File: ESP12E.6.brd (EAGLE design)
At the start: 36.6 x 36.6 mm, 64 parts, among them CN2 1X4-BIG, J1 1X2-3.5MM, J4 1X2-3.5MM, U1 A5984

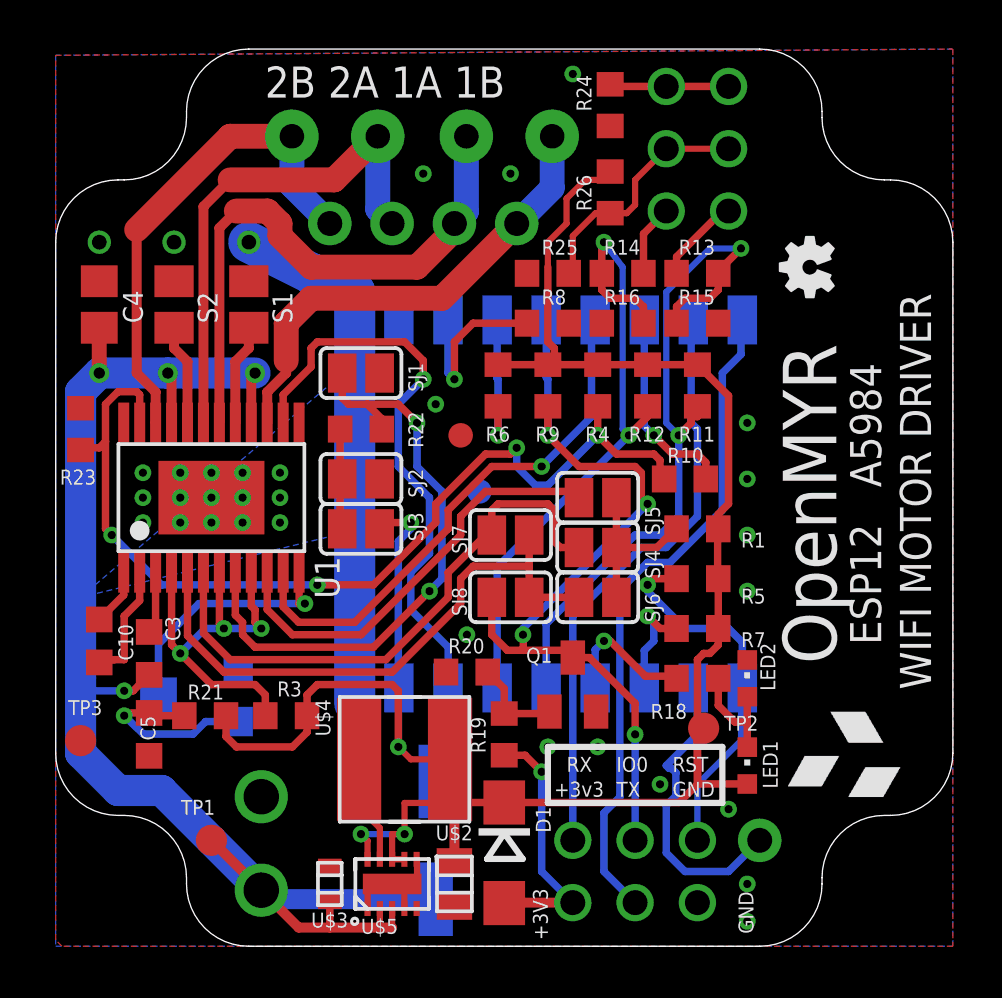
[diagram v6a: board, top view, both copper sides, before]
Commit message: A5984 QFN24
Layout with QFN24 driver
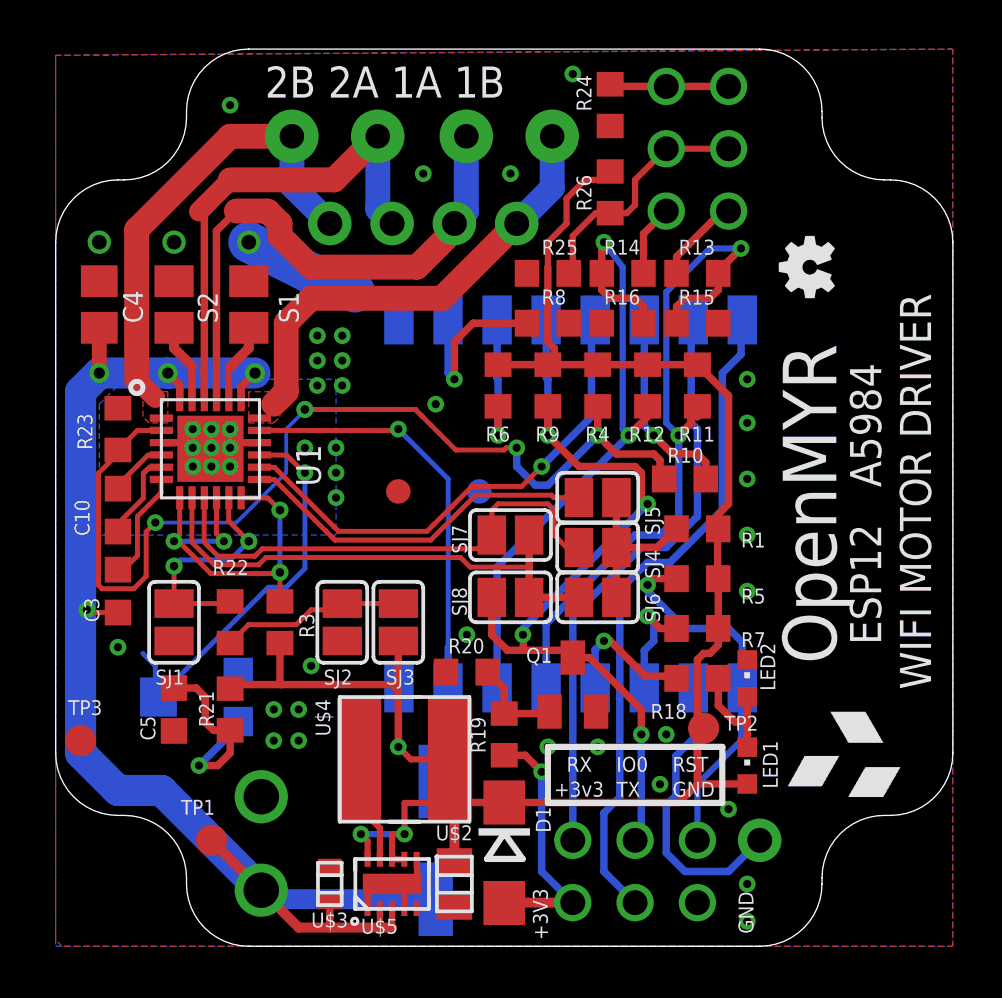
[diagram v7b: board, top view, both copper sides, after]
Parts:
- U1: device A5984:TSSOP-28 -> A5984:QFN-24
- moved SJ1 12.7 mm to (4.83, 13.2), turned to 90 degrees
- moved R22 9.51 mm to (7.11, 13.2), turned to 90 degrees
- moved SJ2 5.89 mm to (11.7, 13.2), turned to 90 degrees
- moved C10 5.39 mm to (2.54, 17.8)
- moved SJ3 4.10 mm to (14.0, 13.2), turned to 270 degrees
- moved R3 3.82 mm to (9.14, 13.2), turned to 90 degrees
- moved FD2 3.42 mm to (14.0, 18.5)
- moved C3 2.84 mm to (2.54, 14.5)
- moved U1 2.03 mm to (6.35, 20.3)
- moved R23 1.52 mm to (2.54, 21.1)
- moved C5 1.44 mm to (4.83, 9.65)
- moved R21 1.05 mm to (7.11, 9.65), turned to 90 degrees
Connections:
- net 1A: now also U1.P$21; no longer U1.18
- net 1B: now also U1.P$18; no longer U1.15
- net 2A: now also U1.P$22; no longer U1.19
- net 2B: now also U1.P$1; no longer U1.22
- net GND: now also U1.P$16, U1.P$25, U1.P$3; no longer U1.13, U1.24, U1.EXP
- net N$11: now also U1.P$6; no longer U1.3
- net N$6: now also U1.P$4; no longer U1.1
- net N$8: now also U1.P$5; no longer U1.2
- net ROSC: now also U1.P$11; no longer U1.8
- net SA: now also U1.P$20; no longer U1.17
- net SB: now also U1.P$23; no longer U1.20
- net VMOT: now also U1.P$19, U1.P$24; no longer U1.16, U1.21
- net VREF: now also U1.P$15; no longer U1.12
- net XDIR: now also U1.P$17; no longer U1.14
- net XENABLE: now also U1.P$2; no longer U1.23
- net XMS1: now also U1.P$8; no longer U1.5
- net XMS2: now also U1.P$9; no longer U1.6
- net XMS3: now also U1.P$13; no longer U1.10
- net XRESET: now also U1.P$10, U1.P$12, U1.P$7; no longer U1.4, U1.7, U1.9
- net XSTEP: now also U1.P$14; no longer U1.11
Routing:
- net ROSC: track 24.7 -> 10.0 mm
- net GND: track 26.7 -> 12.6 mm, vias 34 -> 47
- net +3V3: track 89.5 -> 82.2 mm, vias 4 -> 3
- net XDIR: track 23.7 -> 17.1 mm
- net VREF: track 10.3 -> 16.2 mm
- net XMS1: track 24.1 -> 20.8 mm
- net N$2: track 4.28 -> 7.48 mm
- net XMS2: track 23.5 -> 20.4 mm
- net XMS3: track 17.6 -> 14.8 mm
- net N$11: track 2.53 -> 4.63 mm
- net XSTEP: track 22.2 -> 20.6 mm
- net XENABLE: track 40.1 -> 41.7 mm
- net VMOT: track 60.4 -> 59.2 mm
- net 2B: track 20.3 -> 19.3 mm
- net N$8: track 4.84 -> 3.85 mm
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- added copper zone on layer 1, net 1B
- added copper zone on layer 1, net 2B
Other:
- board text removed: "Project located at: https://github.com/OpenMYR/ESP12E.6/ Copyright Christopher Adams 2016. Licensed under CERN OHL v.1.2 or later This documentation is distributed WITHOUT ANY EXPRESS OR IMPLIED WARRANTY, INCLUDING OF MERCHANTABILITY, SATISFACTORY QUALITY AND FITNESS FOR A PARTICULAR PURPOSE. Please see the CERN OHL v.1.2 for applicable conditions"
